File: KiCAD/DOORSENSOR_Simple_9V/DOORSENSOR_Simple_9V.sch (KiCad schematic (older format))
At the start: 11 parts, among them J1 Conn_01x02_Female, Q1 NTR4003NT1G, SW1 Trigger, SW2 Open/Close, SW3 Pairing, U1 AMS1117-3.3, U2 ESP-12F

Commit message: Update
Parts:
- J1: value Conn_01x02_Female -> 9V
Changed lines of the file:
@@
 P 800 2250
 F 0 "J1" H 692 1925 50  0000 C CNN
-F 1 "Conn_01x02_Female" H 692 2016 50  0000 C CNN
+F 1 "9V" H 692 2016 50  0000 C CNN
 F 2 "Connector_JST:JST_PH_S2B-PH-K_1x02_P2.00mm_Horizontal" H 800 2250 50  0001 C CNN
 F 3 "~" H 800 2250 50  0001 C CNN

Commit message: Update
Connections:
- net GND: no longer R2.2, SW2.2, SW3.2, U2.15 (GND)
- net at Q1.3 (D), U1.1 (GND): now also R2.2, SW2.2, SW3.2, U2.15 (GND)
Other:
- moved on the sheet: SW2
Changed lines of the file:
@@
 $EndComp
-$Comp
-L power:GND #PWR07
-U 1 1 6077856C
-P 5150 3100
-F 0 "#PWR07" H 5150 2850 50  0001 C CNN
-F 1 "GND" H 5155 2927 50  0000 C CNN
-F 2 "" H 5150 3100 50  0001 C CNN
-F 3 "" H 5150 3100 50  0001 C CNN
-	1    5150 3100
-	1    0    0    -1
-$EndComp
-Wire Wire Line
-	5150 3050 5150 3100
 $Comp
 L Switch:SW_Reed SW2
 U 1 1 607790E4
-P 6250 2900
-F 0 "SW2" V 6204 2985 50  0000 L CNN
-F 1 "Open/Close" V 6295 2985 50  0000 L CNN
-F 2 "SHRDZM:Magnetic Reed Relay" H 6250 2900 50  0001 C CNN
-F 3 "~" H 6250 2900 50  0001 C CNN
-	1    6250 2900
+P 6250 2850
+F 0 "SW2" V 6204 2935 50  0000 L CNN
+F 1 "Open/Close" V 6295 2935 50  0000 L CNN
+F 2 "SHRDZM:Magnetic Reed Relay" H 6250 2850 50  0001 C CNN
+F 3 "~" H 6250 2850 50  0001 C CNN
+	1    6250 2850
 	0    1    1    0
-$EndComp
-$Comp
-L power:GND #PWR09
-U 1 1 6077A1D1
-P 6250 3100
-F 0 "#PWR09" H 6250 2850 50  0001 C CNN
-F 1 "GND" H 6255 2927 50  0000 C CNN
-F 2 "" H 6250 3100 50  0001 C CNN
-F 3 "" H 6250 3100 50  0001 C CNN
-	1    6250 3100
-	1    0    0    -1
 $EndComp
 $Comp
@@
 Wire Wire Line
 	5950 2650 5950 2750
-$Comp
-L power:GND #PWR08
-U 1 1 6077B6AB
-P 5950 3100
-F 0 "#PWR08" H 5950 2850 50  0001 C CNN
-F 1 "GND" H 5955 2927 50  0000 C CNN
-F 2 "" H 5950 3100 50  0001 C CNN
-F 3 "" H 5950 3100 50  0001 C CNN
-	1    5950 3100
-	1    0    0    -1
-$EndComp
-Wire Wire Line
-	5950 3050 5950 3100
 $Comp
 L eec:NTR4003NT1G Q1
@@
 	6250 2250 5750 2250
 Wire Wire Line
-	6250 2250 6250 2700
-Wire Wire Line
 	5750 2750 5750 3100
 Wire Wire Line
@@
 Wire Wire Line
 	5750 2450 6950 2450
-$Comp
-L power:GND #PWR010
-U 1 1 60793010
-P 6950 3100
-F 0 "#PWR010" H 6950 2850 50  0001 C CNN
-F 1 "GND" H 6955 2927 50  0000 C CNN
-F 2 "" H 6950 3100 50  0001 C CNN
-F 3 "" H 6950 3100 50  0001 C CNN
-	1    6950 3100
-	1    0    0    -1
-$EndComp
 Wire Wire Line
 	6950 2450 6950 2550
-Wire Wire Line
-	6950 2950 6950 3100
 NoConn ~ 4550 2850
 NoConn ~ 4550 2750
@@
 Wire Wire Line
 	1000 1600 1000 2150
+Wire Wire Line
+	5150 3050 3600 3050
+Wire Wire Line
+	3600 3050 3600 2150
+Connection ~ 3600 2150
+Wire Wire Line
+	5950 3050 5150 3050
+Connection ~ 5150 3050
+Wire Wire Line
+	6250 3050 5950 3050
+Connection ~ 5950 3050
+Wire Wire Line
+	6950 2950 6950 3050
+Wire Wire Line
+	6950 3050 6250 3050
+Connection ~ 6250 3050
+Wire Wire Line
+	6250 2250 6250 2650
 $EndSCHEMATC

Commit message: Update
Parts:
- Q1: symbol eec:NTR4003NT1G -> DOORSENSOR_Simple_9V-rescue:NTR4003NT1G-eec
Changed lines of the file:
@@
 L power:GND #PWR02
 U 1 1 60772F57
-P 1000 3100
-F 0 "#PWR02" H 1000 2850 50  0001 C CNN
-F 1 "GND" H 1005 2927 50  0000 C CNN
-F 2 "" H 1000 3100 50  0001 C CNN
-F 3 "" H 1000 3100 50  0001 C CNN
-	1    1000 3100
+P 1000 3250
+F 0 "#PWR02" H 1000 3000 50  0001 C CNN
+F 1 "GND" H 1005 3077 50  0000 C CNN
+F 2 "" H 1000 3250 50  0001 C CNN
+F 3 "" H 1000 3250 50  0001 C CNN
+	1    1000 3250
 	1    0    0    -1
 $EndComp
@@
 L power:GND #PWR03
 U 1 1 60773683
-P 1700 3100
-F 0 "#PWR03" H 1700 2850 50  0001 C CNN
-F 1 "GND" H 1705 2927 50  0000 C CNN
-F 2 "" H 1700 3100 50  0001 C CNN
-F 3 "" H 1700 3100 50  0001 C CNN
-	1    1700 3100
-	1    0    0    -1
-$EndComp
-Wire Wire Line
-	1700 2750 1700 3100
+P 1700 3250
+F 0 "#PWR03" H 1700 3000 50  0001 C CNN
+F 1 "GND" H 1705 3077 50  0000 C CNN
+F 2 "" H 1700 3250 50  0001 C CNN
+F 3 "" H 1700 3250 50  0001 C CNN
+	1    1700 3250
+	1    0    0    -1
+$EndComp
 $Comp
 L Device:R R1
@@
 L power:GND #PWR04
 U 1 1 60774281
-P 2150 3100
-F 0 "#PWR04" H 2150 2850 50  0001 C CNN
-F 1 "GND" H 2155 2927 50  0000 C CNN
-F 2 "" H 2150 3100 50  0001 C CNN
-F 3 "" H 2150 3100 50  0001 C CNN
-	1    2150 3100
-	1    0    0    -1
-$EndComp
-Wire Wire Line
-	2150 2750 2150 3100
+P 2150 3250
+F 0 "#PWR04" H 2150 3000 50  0001 C CNN
+F 1 "GND" H 2155 3077 50  0000 C CNN
+F 2 "" H 2150 3250 50  0001 C CNN
+F 3 "" H 2150 3250 50  0001 C CNN
+	1    2150 3250
+	1    0    0    -1
+$EndComp
 $Comp
 L power:GND #PWR05
 U 1 1 60774757
-P 2800 3100
-F 0 "#PWR05" H 2800 2850 50  0001 C CNN
-F 1 "GND" H 2805 2927 50  0000 C CNN
-F 2 "" H 2800 3100 50  0001 C CNN
-F 3 "" H 2800 3100 50  0001 C CNN
-	1    2800 3100
+P 2800 3250
+F 0 "#PWR05" H 2800 3000 50  0001 C CNN
+F 1 "GND" H 2805 3077 50  0000 C CNN
+F 2 "" H 2800 3250 50  0001 C CNN
+F 3 "" H 2800 3250 50  0001 C CNN
+	1    2800 3250
 	1    0    0    -1
 $EndComp
@@
 	5950 2650 5950 2750
 $Comp
-L eec:NTR4003NT1G Q1
+L DOORSENSOR_Simple_9V-rescue:NTR4003NT1G-eec Q1
 U 1 1 60784E62
 P 2200 2250
@@
 $EndComp
 Wire Wire Line
-	2800 2650 2800 3100
-Wire Wire Line
 	1700 1600 2800 1600
 Wire Wire Line
@@
 L power:GND #PWR06
 U 1 1 6078E715
-P 3900 3100
-F 0 "#PWR06" H 3900 2850 50  0001 C CNN
-F 1 "GND" H 3905 2927 50  0000 C CNN
-F 2 "" H 3900 3100 50  0001 C CNN
-F 3 "" H 3900 3100 50  0001 C CNN
-	1    3900 3100
-	1    0    0    -1
-$EndComp
-Wire Wire Line
-	3900 2800 3900 3100
+P 3900 3250
+F 0 "#PWR06" H 3900 3000 50  0001 C CNN
+F 1 "GND" H 3905 3077 50  0000 C CNN
+F 2 "" H 3900 3250 50  0001 C CNN
+F 3 "" H 3900 3250 50  0001 C CNN
+	1    3900 3250
+	1    0    0    -1
+$EndComp
 Wire Wire Line
 	3900 1850 4150 1850
@@
 	750  3000 1000 3000
 Connection ~ 1000 3000
-Wire Wire Line
-	1000 3000 1000 3100
 $Comp
 L power:PWR_FLAG #FLG01
@@
 Wire Wire Line
 	1000 1600 1000 2150
-Wire Wire Line
-	5150 3050 3600 3050
-Wire Wire Line
-	3600 3050 3600 2150
 Connection ~ 3600 2150
 Wire Wire Line
-	5950 3050 5150 3050
-Connection ~ 5150 3050
-Wire Wire Line
-	6250 3050 5950 3050
-Connection ~ 5950 3050
-Wire Wire Line
-	6950 2950 6950 3050
-Wire Wire Line
-	6950 3050 6250 3050
-Connection ~ 6250 3050
-Wire Wire Line
 	6250 2250 6250 2650
+Wire Wire Line
+	3900 2800 3900 3250
+Wire Wire Line
+	2800 2650 2800 3250
+Wire Wire Line
+	2150 2750 2150 3250
+Wire Wire Line
+	1700 2750 1700 3250
+Wire Wire Line
+	1000 3000 1000 3250
+Wire Wire Line
+	3600 3200 5150 3200
+Wire Wire Line
+	3600 2150 3600 3200
+Wire Wire Line
+	6950 2950 6950 3200
+Wire Wire Line
+	6250 3050 6250 3200
+Connection ~ 6250 3200
+Wire Wire Line
+	6250 3200 6950 3200
+Wire Wire Line
+	5950 3050 5950 3200
+Connection ~ 5950 3200
+Wire Wire Line
+	5950 3200 6250 3200
+Wire Wire Line
+	5150 3050 5150 3200
+Connection ~ 5150 3200
+Wire Wire Line
+	5150 3200 5950 3200
 $EndSCHEMATC

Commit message: Update
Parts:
- added R3: 1.8k, symbol Device:R
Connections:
- net at C1.1, Q1.1 (G), R1.1: now also R3.2; no longer SW1.2
- new net: R3.1, SW1.2
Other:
- moved on the sheet: C1, Q1, R1, SW1

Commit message: Update
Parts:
- R3: footprint (none) -> Resistor_SMD:R_0805_2012Metric_Pad1.20x1.40mm_HandSolder
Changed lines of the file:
@@
 F 0 "R3" H 1770 2196 50  0000 L CNN
 F 1 "1.8k" H 1770 2105 50  0000 L CNN
-F 2 "" V 1630 2150 50  0001 C CNN
+F 2 "Resistor_SMD:R_0805_2012Metric_Pad1.20x1.40mm_HandSolder" V 1630 2150 50  0001 C CNN
 F 3 "~" H 1700 2150 50  0001 C CNN
 	1    1700 2150

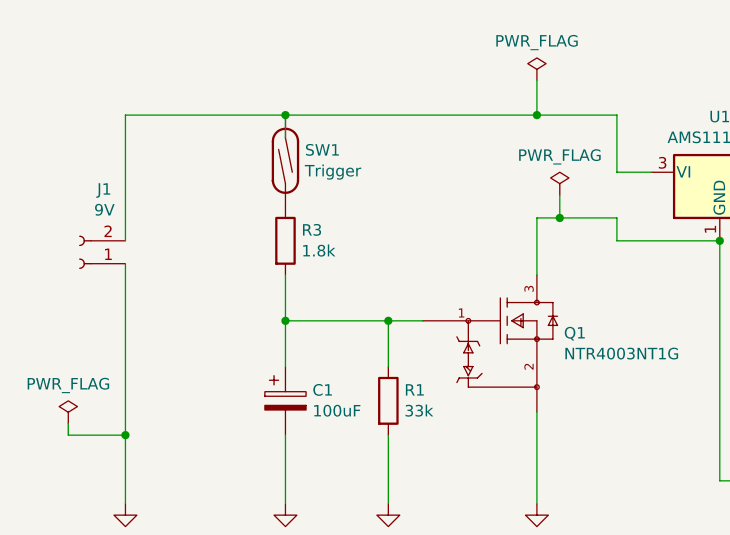
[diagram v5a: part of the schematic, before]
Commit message: Website last measurement values added
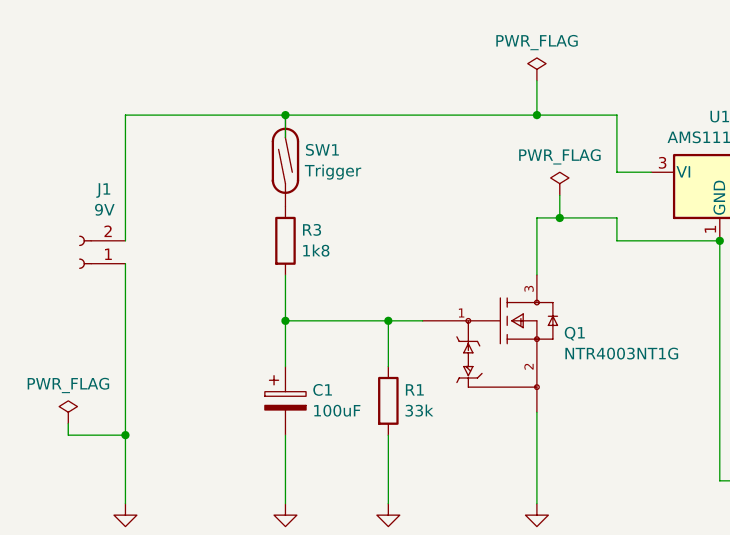
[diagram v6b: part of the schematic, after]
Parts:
- R3: value 1.8k -> 1k8
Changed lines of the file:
@@
 P 1700 2150
 F 0 "R3" H 1770 2196 50  0000 L CNN
-F 1 "1.8k" H 1770 2105 50  0000 L CNN
+F 1 "1k8" H 1770 2105 50  0000 L CNN
 F 2 "Resistor_SMD:R_0805_2012Metric_Pad1.20x1.40mm_HandSolder" V 1630 2150 50  0001 C CNN
 F 3 "~" H 1700 2150 50  0001 C CNN
